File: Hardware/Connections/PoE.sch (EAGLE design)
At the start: 4 parts

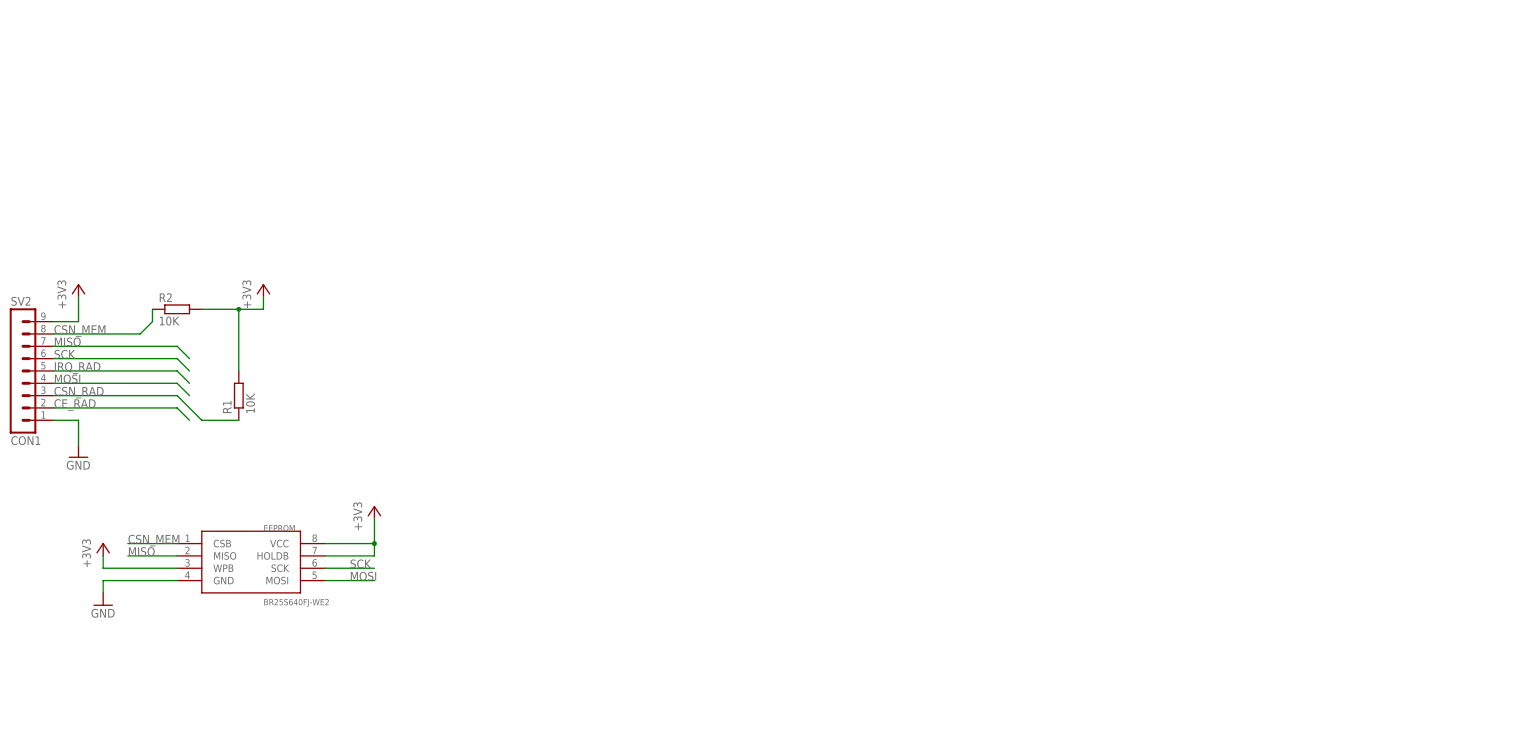
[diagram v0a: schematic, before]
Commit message: updated PoE Schematic slightly and added eagle project file. Updated Readme to explain current directory structure
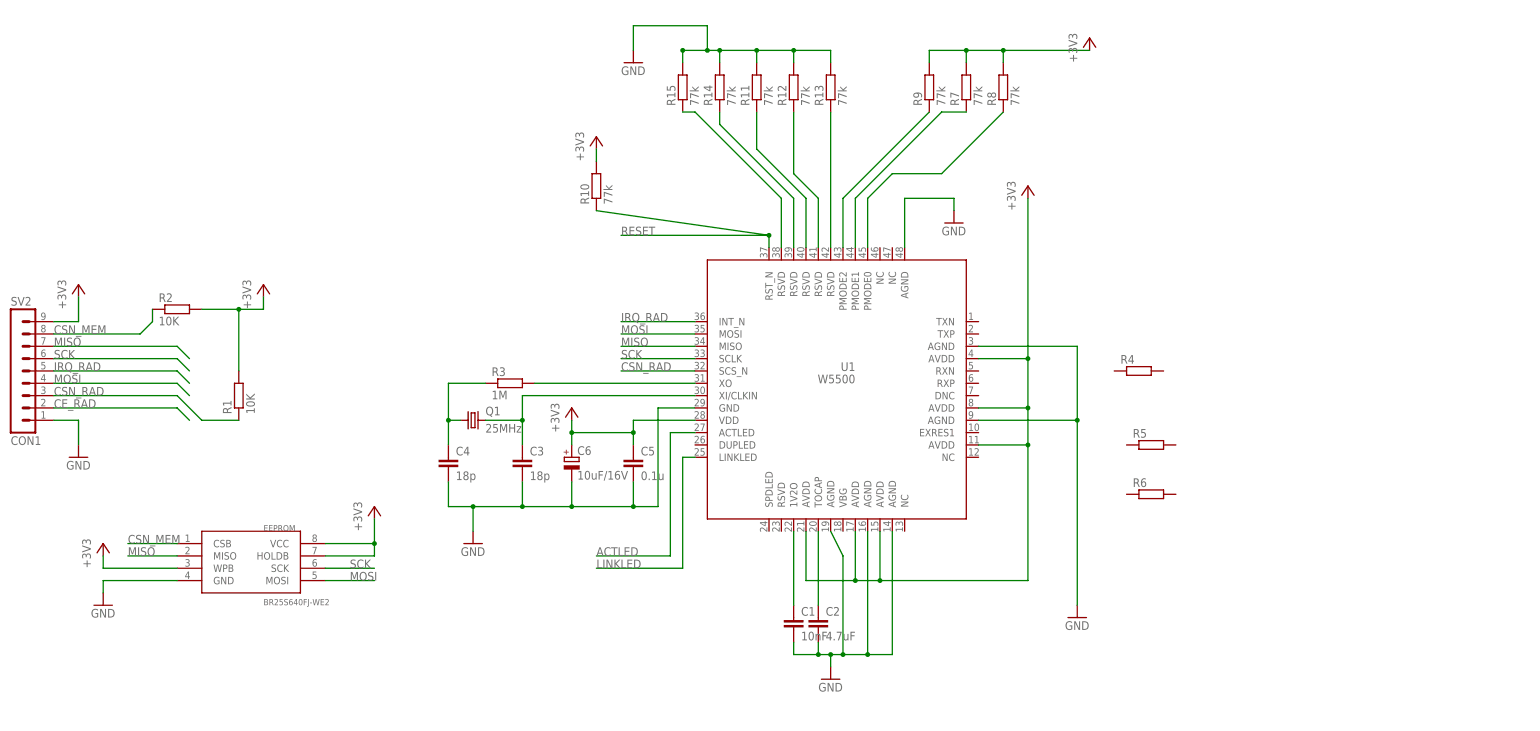
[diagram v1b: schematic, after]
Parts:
- added C1: 10nF, rcl:C-EUC1206
- added C2: 4.7uF, rcl:C-EUC1206
- added C3, C4: 18p, rcl:C-EUC1206
- added C5: 0.1u, rcl:C-EUC1206
- added C6: 10uF/16V, rcl:CPOL-EU140CLH-1010
- added Q1: 25MHz, crystal:CRYSTALHC49UP
- added R10, R11, R12, R13, R14, R15, R7, R8, R9: 77k, resistor:R-EU_R1206
- added R3: 1M, resistor:R-EU_R1206
- added R4, R5, R6: (no value), resistor:R-EU_R1206
- added U1: W5500, W5500:W5500
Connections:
- new net ACTLED: U1.ACTLED
- new net LINKLED: U1.LINKLED
- new net N$1: R9.1, U1.PMODE2
- new net N$10: R14.1, U1.RSVD@3
- new net N$11: R11.1, U1.RSVD@4
- new net N$12: R12.1, U1.RSVD@5
- new net N$13: R13.1, U1.RSVD@6
- new net N$2: C1.1, U1.1V2O
- new net N$3: C2.1, U1.TOCAP
- new net N$4: C4.1, Q1.1, R3.1
- new net N$5: C3.1, Q1.2, U1.XI/CLKIN
- new net N$6: R7.1, U1.PMODE1
- new net N$7: R3.2, U1.XO
- new net N$8: R8.1, U1.PMODE0
- new net N$9: R15.1, U1.RSVD@2
- new net RESET: R10.1, U1.RST_N
- net +3V3: now also C5.1, C6.+, R10.2, R7.2, R8.2, R9.2, U1.AVDD@1, U1.AVDD@2, U1.AVDD@3, U1.AVDD@4, U1.AVDD@5, U1.AVDD@6, U1.VDD
- net CSN_RAD: now also U1.SCS_N
- net GND: now also C1.2, C2.2, C3.2, C4.2, C5.2, C6.-, R11.2, R12.2, R13.2, R14.2, R15.2, U1.AGND@1, U1.AGND@2, U1.AGND@3, U1.AGND@4, U1.AGND@5, U1.AGND@6, U1.GND
- net IRQ_RAD: now also U1.INT_N
- net MISO: now also U1.MISO
- net MOSI: now also U1.MOSI
- net SCK: now also U1.SCLK

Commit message: updated POE design. missing power circuitry and suitable rj45 connector
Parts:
- added C10, C11: 6.8, rcl:C-EUC1206
- added C12, C13, C14, C15, C16, C17: 0.1u, rcl:C-EUC1206
- added C18: 10uF/16V, rcl:CPOL-EU153CLV-0405
- added C7: 1nF/2kV, rcl:C-EUC1206
- added C8: 22n, rcl:C-EUC1206
- added C9: 10n, rcl:C-EUC1206
- added L1: (no value), inductor-neosid:MS50
- added R16, R17: 49R9 1%, resistor:R-EU_R1206
- added R18: 12.4k 1%, resistor:R-EU_R1206
- added R19, R20: 330R, resistor:R-EU_R1206
- C6: device rcl:CPOL-EU140CLH-1010 -> rcl:CPOL-EU153CLV-0505
- R4, R5: value (none) -> 49R9 1%
- R6: value (none) -> 10R 1%
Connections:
- new net GNDA: C7.2
- new net N$14: R5.1, U1.TXP
- new net N$16: C8.1, R6.1
- new net N$17: R4.1, U1.TXN
- new net N$18: C10.1, R16.2, U1.RXP
- new net N$19: C9.1, R16.1, R17.1
- new net N$20: C11.2
- new net N$21: C10.2
- new net N$22: R18.2, U1.EXRES1
- new net VDD: C12.1, C13.1, C14.1, C15.1, C16.1, C17.1, C18.+, L1.2, R4.2, R5.2, R6.2, U1.AVDD@1, U1.AVDD@2, U1.AVDD@3, U1.AVDD@4, U1.AVDD@5, U1.AVDD@6
- net +3V3: now also L1.1; no longer U1.AVDD@1, U1.AVDD@2, U1.AVDD@3, U1.AVDD@4, U1.AVDD@5, U1.AVDD@6
- net GND: now also C1.1, C12.2, C13.2, C14.2, C15.2, C16.2, C17.2, C18.-, C7.1, C8.2, C9.2, R18.1; no longer C1.2
- net N$2: now also C1.2; no longer C1.1
- net N$4: now also U1.XO
- net N$5: now also R3.2
- net N$7: now also C11.1, R17.2, U1.RXN; no longer R3.2, U1.XO
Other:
- moved on the sheet: C1, C2, C3, C4, Q1, R10, R3, R4, R5, R6
